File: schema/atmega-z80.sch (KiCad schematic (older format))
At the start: 68 parts, among them J1 USB Connector, J2 Programmer ISP 10, J3 SPI Connector, J4 I2C Connector, Q1 PNP_2N4403, Q2 PNP_2N4403, Q3 NPN_2N4401, Q4 PNP_2N4403, U1 Z84C0010PEG, U2 ATmega324A-PU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

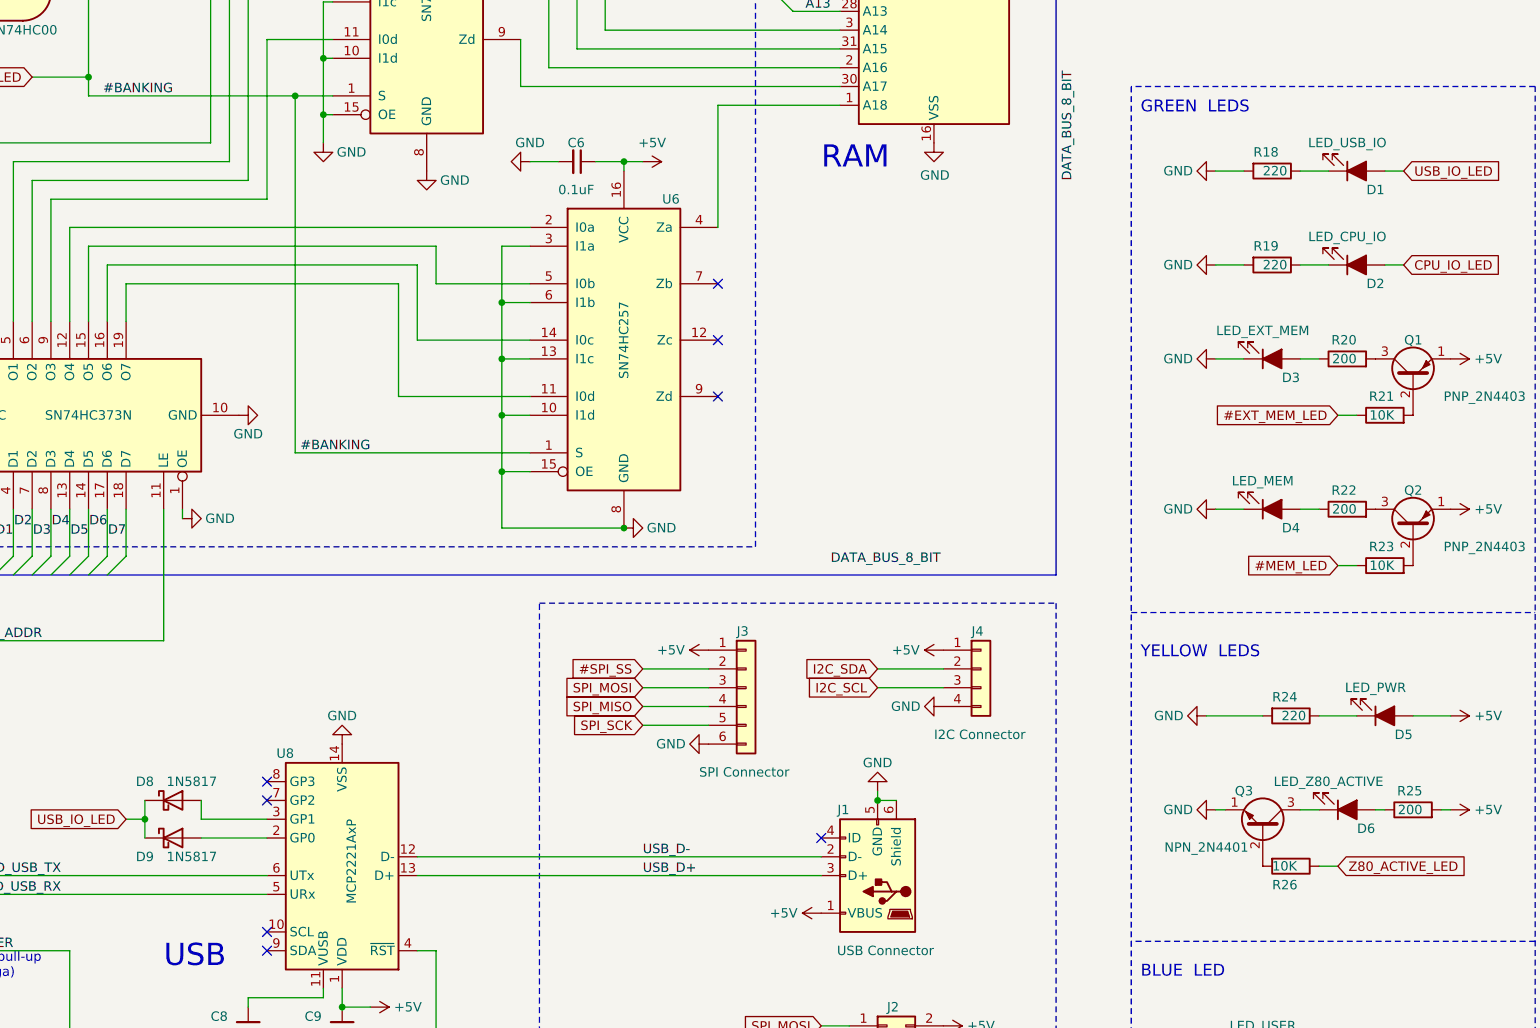
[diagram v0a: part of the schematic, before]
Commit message: Reversed all diodes on line USB_IO_LED because GP0 and GP1 of U8 are active low. (#4)
More PCB layout stuff.
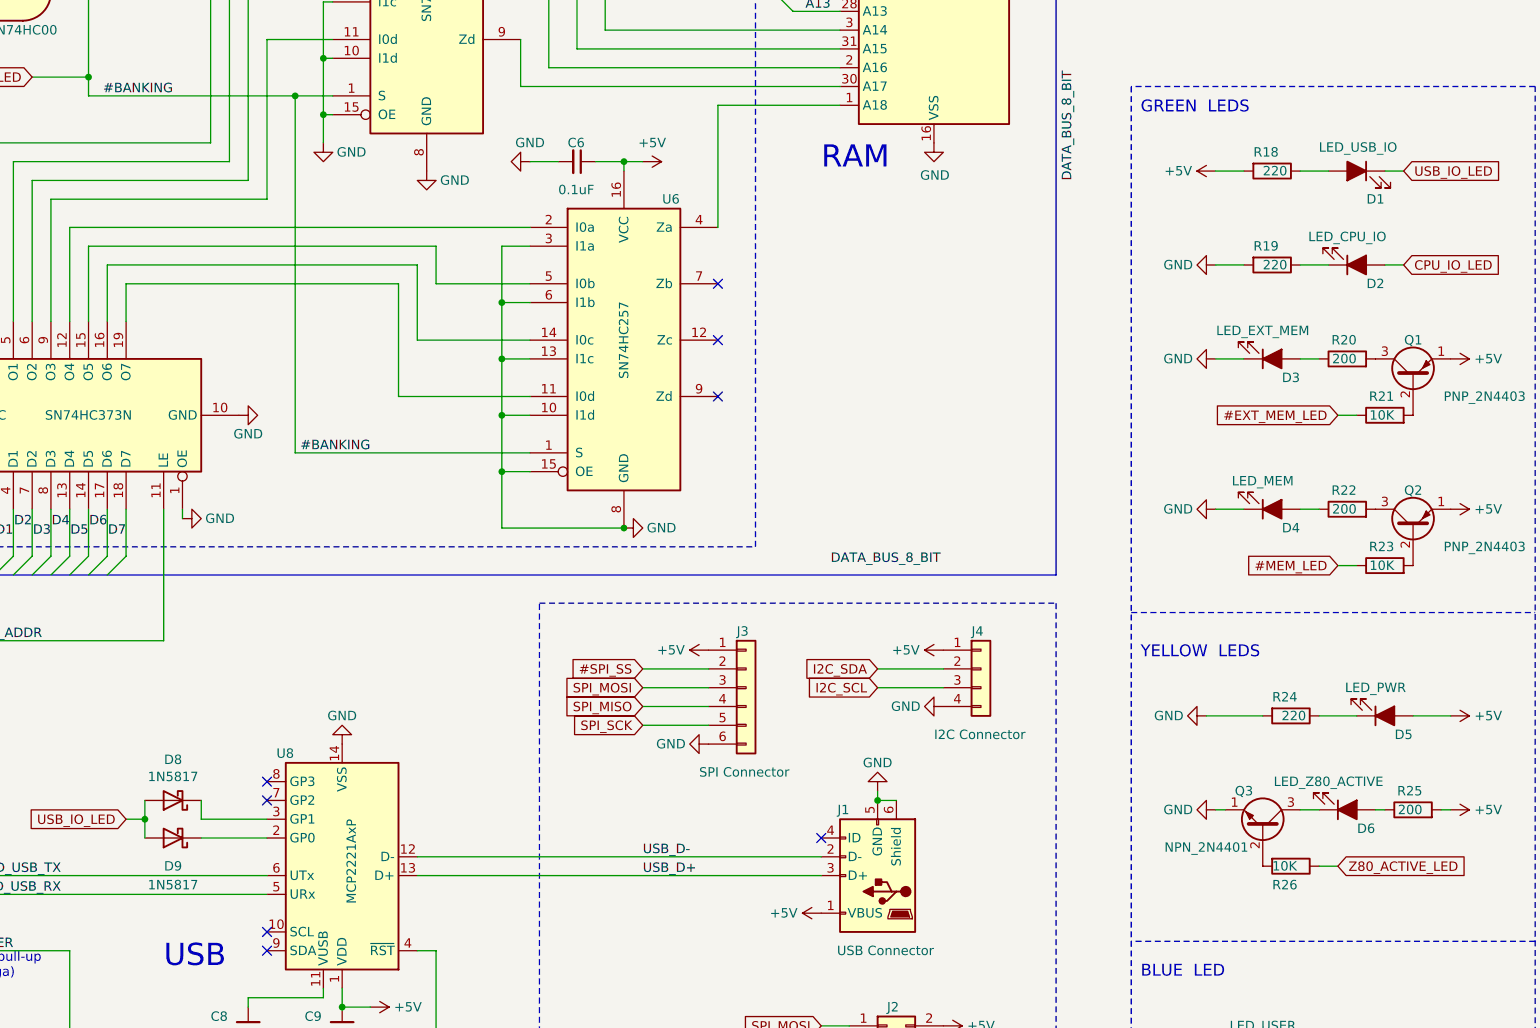
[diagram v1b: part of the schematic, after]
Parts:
- Q1, Q2, Q4: footprint Package_TO_SOT_THT:TO-92 -> Package_TO_SOT_THT:TO-92_Inline
- Q3: footprint Package_TO_SOT_THT:TO-92 -> Package_TO_SOT_THT:TO-92_Inline_Wide
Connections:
- net +5V: now also R18.2
- net GND: no longer R18.2
- net USB_IO_LED: now also D1.1 (K), D8.2 (A), D9.2 (A); no longer D1.2 (A), D8.1 (K), D9.1 (K)
- net at U8.2 (GP0): now also D9.1 (K); no longer D9.2 (A)
- net at U8.3 (GP1): now also D8.1 (K); no longer D8.2 (A)
- net at R18.1: now also D1.2 (A); no longer D1.1 (K)
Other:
- moved on the sheet: D1
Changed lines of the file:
@@
 F 0 "Q3" V 14700 7950 50  0000 C CNN
 F 1 "NPN_2N4401" V 14400 7750 50  0000 C CNN
-F 2 "Package_TO_SOT_THT:TO-92" H 14700 8150 50  0001 C CNN
+F 2 "Package_TO_SOT_THT:TO-92_Inline_Wide" H 14700 8150 50  0001 C CNN
 F 3 "~" H 14500 8050 50  0001 C CNN
 	1    14500 8050
@@
 U 1 1 61EB9A16
 P 15000 4550
-F 0 "D1" H 15100 4650 50  0000 C CNN
-F 1 "LED_USB_IO" H 14950 4400 50  0000 C CNN
+F 0 "D1" H 14900 4400 50  0000 C CNN
+F 1 "LED_USB_IO" H 14993 4676 50  0000 C CNN
 F 2 "LED_THT:LED_D5.0mm" H 15000 4550 50  0001 C CNN
 F 3 "~" H 15000 4550 50  0001 C CNN
 	1    15000 4550
-	1    0    0    1
+	-1   0    0    -1
 $EndComp
 Wire Wire Line
@@
 Wire Wire Line
 	14400 4550 14250 4550
-$Comp
-L power:GND #PWR0127
-U 1 1 61EB9A22
-P 14250 4550
-F 0 "#PWR0127" H 14250 4300 50  0001 C CNN
-F 1 "GND" V 14250 4350 50  0000 C CNN
-F 2 "" H 14250 4550 50  0001 C CNN
-F 3 "" H 14250 4550 50  0001 C CNN
-	1    14250 4550
-	0    1    1    0
-$EndComp
 Wire Wire Line
 	14400 5050 14250 5050
@@
 F 0 "Q1" V 15500 5600 50  0000 L CNN
 F 1 "PNP_2N4403" V 15200 5050 50  0000 L CNN
-F 2 "Package_TO_SOT_THT:TO-92" H 15500 5750 50  0001 C CNN
+F 2 "Package_TO_SOT_THT:TO-92_Inline" H 15500 5750 50  0001 C CNN
 F 3 "~" H 15300 5650 50  0001 C CNN
 	1    15300 5650
@@
 F 0 "Q2" V 15500 6400 50  0000 L CNN
 F 1 "PNP_2N4403" V 15200 5850 50  0000 L CNN
-F 2 "Package_TO_SOT_THT:TO-92" H 15500 6550 50  0001 C CNN
+F 2 "Package_TO_SOT_THT:TO-92_Inline" H 15500 6550 50  0001 C CNN
 F 3 "~" H 15300 6450 50  0001 C CNN
 	1    15300 6450
@@
 F 0 "Q4" V 15500 9300 50  0000 L CNN
 F 1 "PNP_2N4403" V 15200 8750 50  0000 L CNN
-F 2 "Package_TO_SOT_THT:TO-92" H 15500 9450 50  0001 C CNN
+F 2 "Package_TO_SOT_THT:TO-92_Inline" H 15500 9450 50  0001 C CNN
 F 3 "~" H 15300 9350 50  0001 C CNN
 	1    15300 9350
@@
 U 1 1 61418E5F
 P 8700 8100
-F 0 "D9" H 8550 8000 50  0000 C CNN
-F 1 "1N5817" H 8800 8000 50  0000 C CNN
+F 0 "D9" H 8700 8250 50  0000 C CNN
+F 1 "1N5817" H 8700 8350 50  0000 C CNN
 F 2 "Diode_THT:D_DO-41_SOD81_P10.16mm_Horizontal" H 8700 7925 50  0001 C CNN
 F 3 "http://www.vishay.com/docs/88525/1n5817.pdf" H 8700 8100 50  0001 C CNN
 	1    8700 8100
-	1    0    0    -1
+	-1   0    0    1
 $EndComp
 $Comp
@@
 U 1 1 6141BB94
 P 8700 7900
-F 0 "D8" H 8550 8000 50  0000 C CNN
-F 1 "1N5817" H 8800 8000 50  0000 C CNN
+F 0 "D8" H 8700 7683 50  0000 C CNN
+F 1 "1N5817" H 8700 7774 50  0000 C CNN
 F 2 "Diode_THT:D_DO-41_SOD81_P10.16mm_Horizontal" H 8700 7725 50  0001 C CNN
 F 3 "http://www.vishay.com/docs/88525/1n5817.pdf" H 8700 7900 50  0001 C CNN
 	1    8700 7900
-	1    0    0    -1
+	-1   0    0    1
 $EndComp
 Wire Wire Line
@@
 Wire Wire Line
 	8550 8000 8550 8100
+$Comp
+L power:+5V #PWR0127
+U 1 1 61449BE9
+P 14250 4550
+F 0 "#PWR0127" H 14250 4400 50  0001 C CNN
+F 1 "+5V" V 14250 4750 50  0000 C CNN
+F 2 "" H 14250 4550 50  0001 C CNN
+F 3 "" H 14250 4550 50  0001 C CNN
+	1    14250 4550
+	0    -1   -1   0
+$EndComp
 Wire Bus Line
 	8550 2100 8550 3250
